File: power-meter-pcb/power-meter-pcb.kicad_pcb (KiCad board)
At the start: 4 copper layers, 23 x 51.5 mm, 56 parts, among them J1 Crank interconnect, J2 Debug, J3 USB4120-03-C_REVA, J4 Battery, J5 Side A, J6 Side B, Q3 AS2302, SW1 EN, SW2 BOOT, U1 TPS613221ADBV, U2 P3T1755, U4 TPD3E001DRLR, U7 ADS1232IPW, U8 ESP32-S3-MINI-1

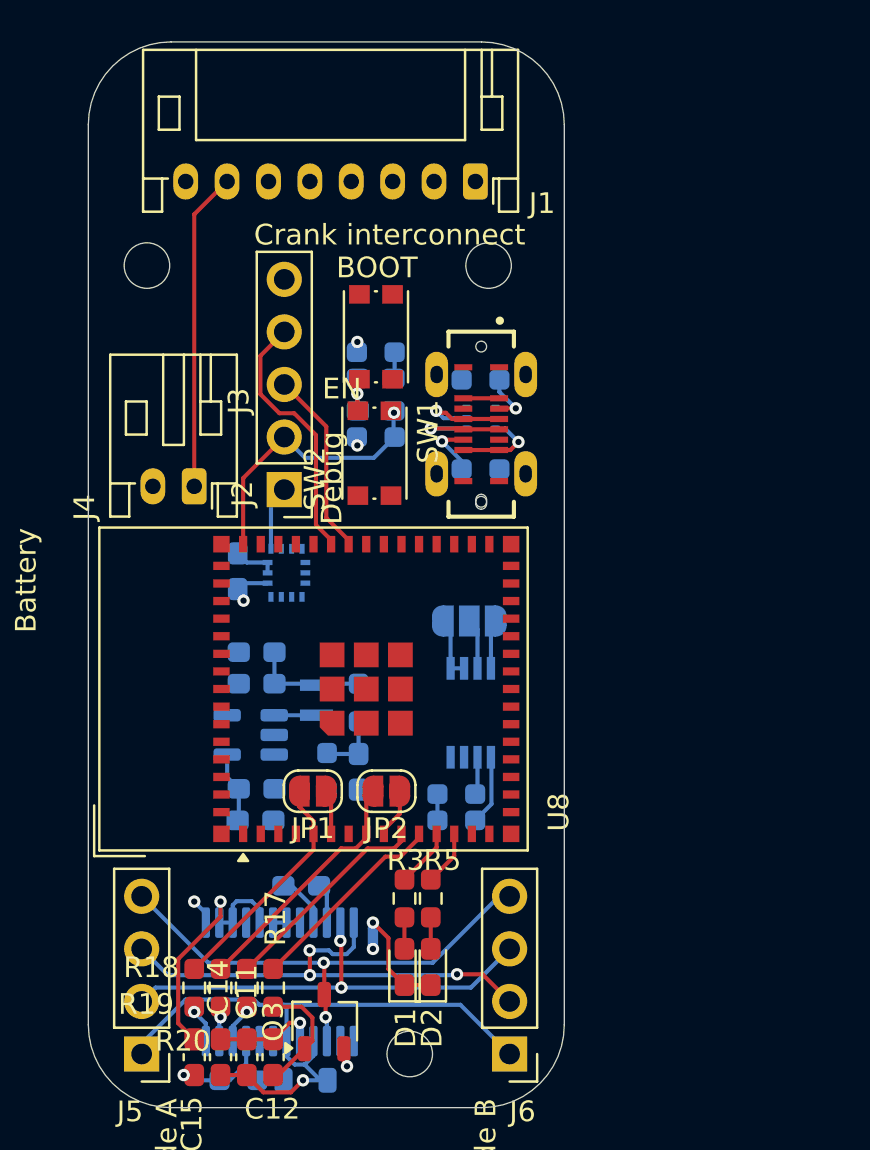
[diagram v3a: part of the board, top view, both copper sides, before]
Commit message: Board mostly routed, schematic page layout cleaned up
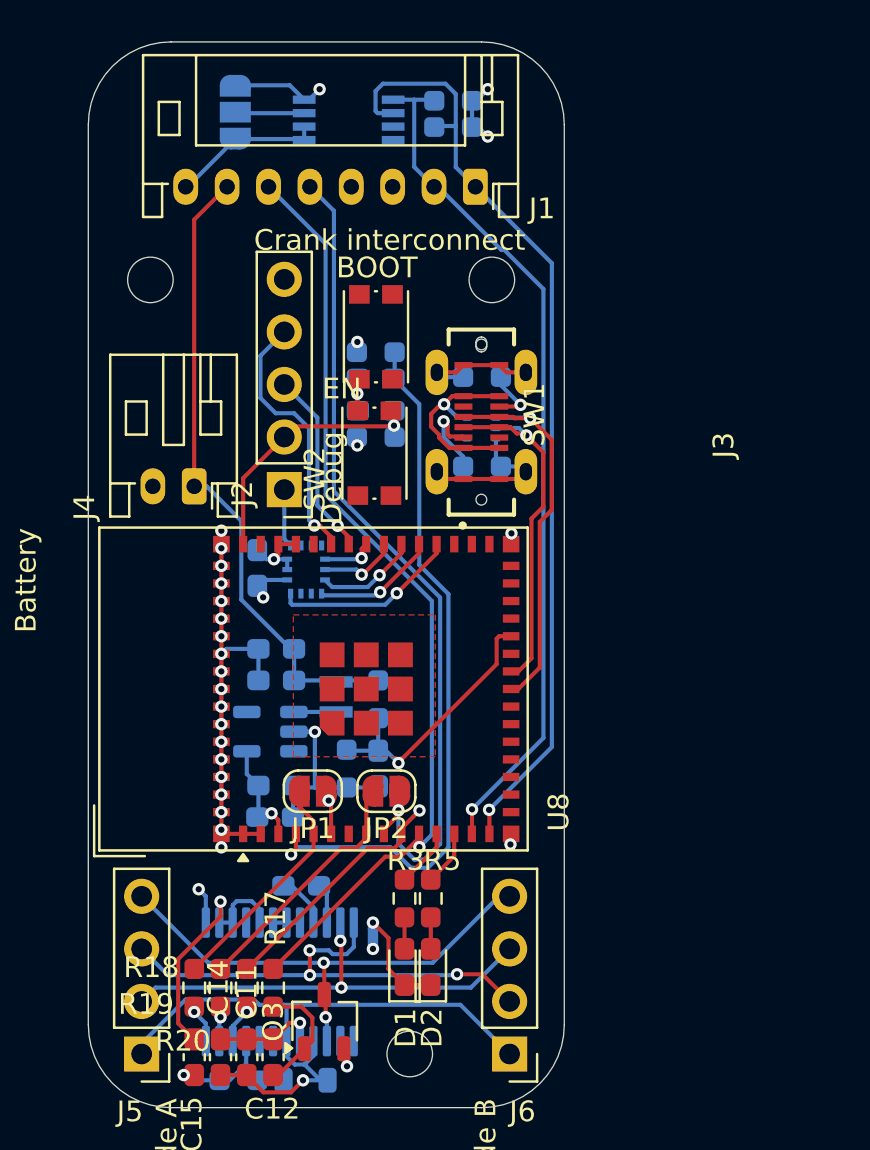
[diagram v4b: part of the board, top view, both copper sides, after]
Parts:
- moved R6 33.5 mm to (74.6, 51.2), turned to 180 degrees
- moved R4 33.5 mm to (74.6, 50.0), turned to 180 degrees
- moved U2 29.3 mm to (69.6, 50.9), turned to 180 degrees
- moved JP3 27.1 mm to (64.1, 50.5), turned to -90 degrees
- moved R11 4.45 mm to (76.0, 63.3), turned to 180 degrees
- moved R8 4.19 mm to (76.0, 67.6), turned to 0 degrees
- moved C10 0.96 mm to (66.1, 83.1)
- moved C16 0.96 mm to (65.2, 72.5)
- moved C5 0.96 mm to (66.1, 76.5)
- moved C7 0.96 mm to (66.1, 78.0)
- moved C8 0.96 mm to (66.0, 84.6)
- moved C9 0.96 mm to (71.0, 82.2)
- moved MT1 0.96 mm to (67.5, 72.6)
- moved R14 0.96 mm to (71.0, 78.9)
- moved R15 0.96 mm to (69.5, 82.2)
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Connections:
- R4 pad 2: /I2C.SDA -> /I2C.SCL
- R6 pad 2: /I2C.SCL -> /I2C.SDA
- U8 pad 14: unconnected-(U8-IO10-Pad14) -> /I2C.SCL
- U8 pad 15: unconnected-(U8-IO11-Pad15) -> /I2C.SDA
- U8 pad 34: unconnected-(U8-IO38-Pad34) -> /Accelerometer/Interrupt
- U8 pad 35: unconnected-(U8-IO39-Pad35) -> /Accelerometer/SPI.SDO
- U8 pad 36: unconnected-(U8-IO40-Pad36) -> /Accelerometer/SPI.SDI
- U8 pad 37: unconnected-(U8-IO41-Pad37) -> /Accelerometer/SPI.SCLK
- U8 pad 38: unconnected-(U8-IO42-Pad38) -> /Accelerometer/SPI.AC_CS
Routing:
- net GNDD: track 28.3 -> 76.8 mm, vias 3 -> 26
- net /I2C.SDA: track 1.82 -> 46.1 mm, vias 0 -> 1
- net /AMP2.DOUT: track 2.16 -> 43.2 mm, vias 0 -> 1
- net /AMP_PWDN: track 10.4 -> 49.9 mm, vias 0 -> 1
- net /AMP2.SCLK: track 2.38 -> 41.0 mm, vias 0 -> 1
- net /I2C.SCL: track 3.38 -> 41.7 mm, vias 0 -> 1
- net /Power save: track 9.87 -> 46.0 mm, vias 0 -> 1
- net /BOOT: track 1.29 -> 34.7 mm, vias 0 -> 1
- net +3.3V: track 20.1 -> 35.7 mm, vias 5 -> 9
- net /USB and power supply/USB.D_N: track 5.05 -> 19.5 mm
- net /USB and power supply/USB.D_P: track 4.82 -> 17.4 mm
- net +BATT: track 21.0 -> 31.3 mm
- net /USB and power supply/Battery voltage: track 3.11 -> 13.1 mm, vias 0 -> 1
- net /Accelerometer/Interrupt: track 0.00 -> 9.02 mm, vias 0 -> 1
- net /Accelerometer/SPI.SDO: track 0.00 -> 6.03 mm, vias 0 -> 1
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- added copper zone on F.Cu, net GNDD

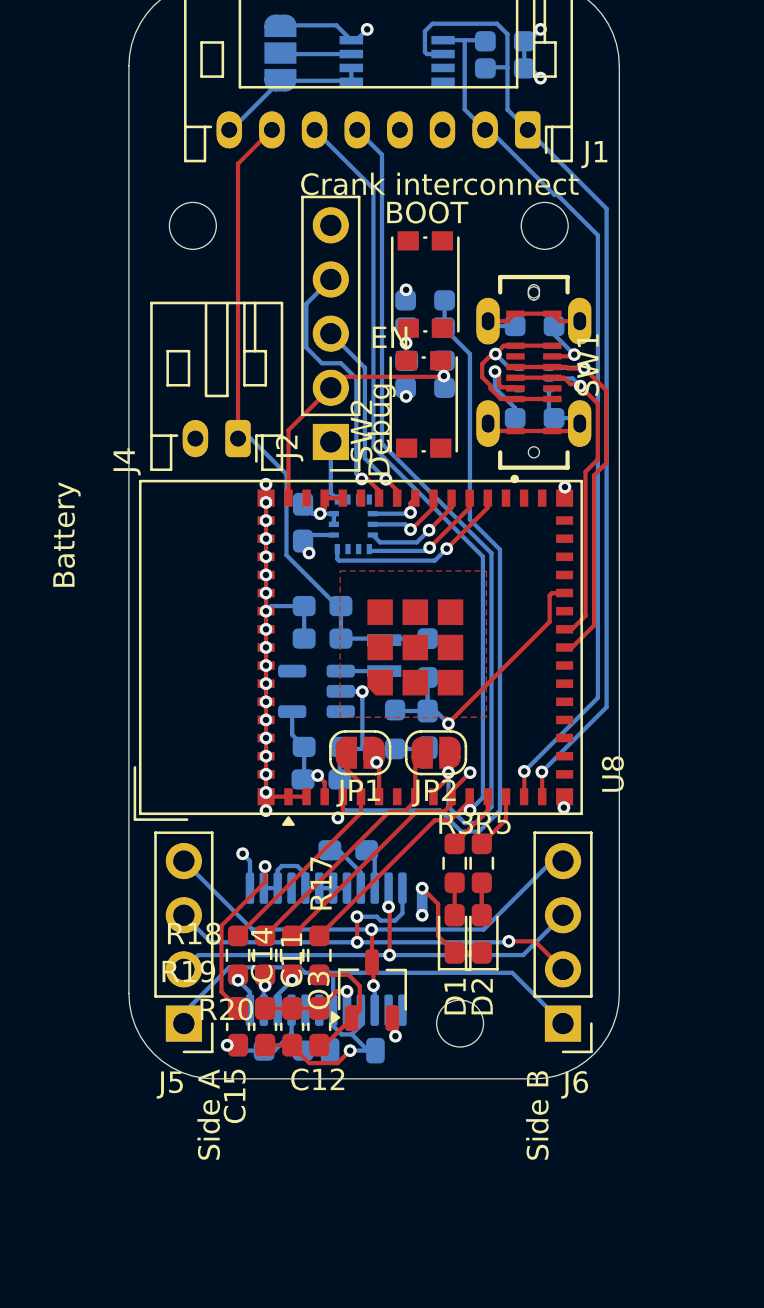
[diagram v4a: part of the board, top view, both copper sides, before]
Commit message: Silkscreen done
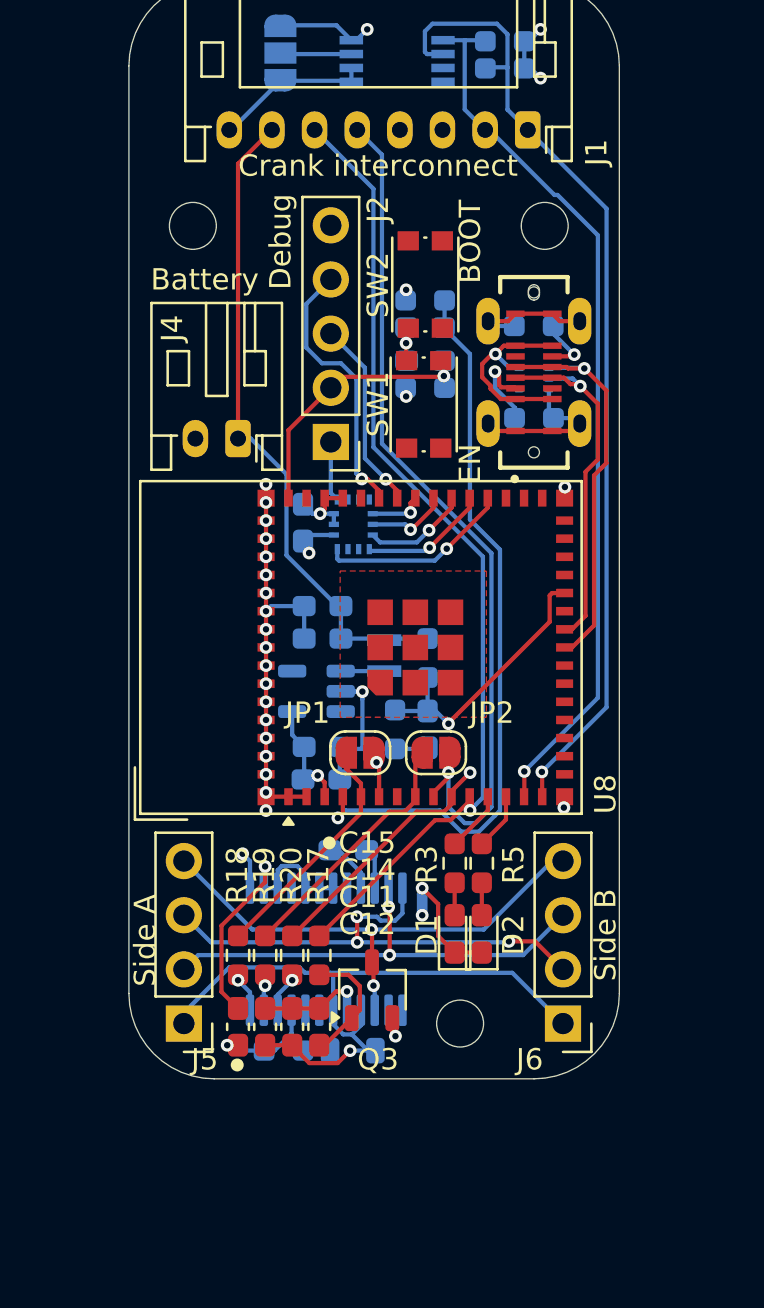
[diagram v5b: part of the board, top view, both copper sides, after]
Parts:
- moved G*** 50.6 mm to (75.2, 75.4), turned to -90 degrees
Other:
- board text added: "+B"
- board text added: "+V"
- board text added: "DOUT"
- board text added: "GND"
- board text added: "J. Gates & O. Varney, 2024"
- board text added: "PS"
- board text added: "PWDN"
- board text added: "SCL"
- board text added: "SCLK"
- board text added: "SDA"
- board text removed: "3.3V"
- board text removed: "G"
- board text removed: "Jotham Gates & Oscar Varney, 2024"

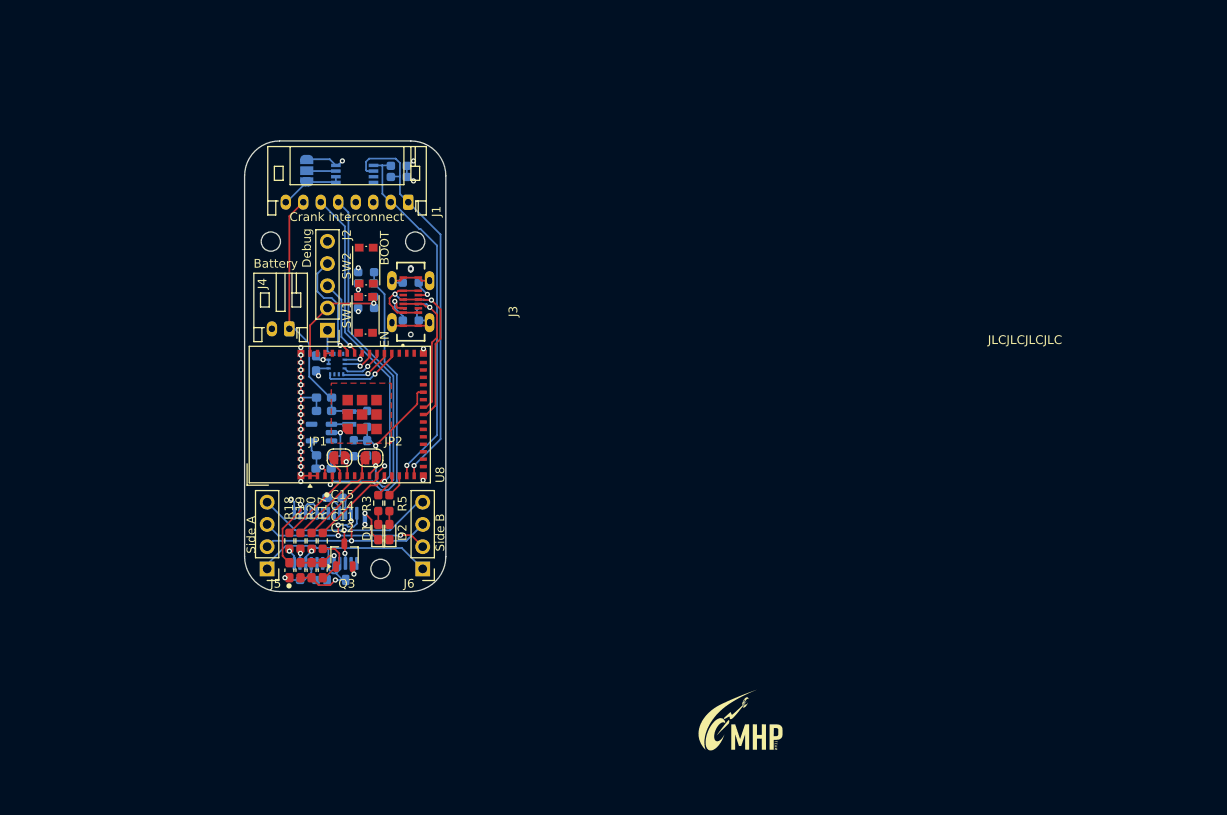
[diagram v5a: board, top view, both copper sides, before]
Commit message: Added date updating script.
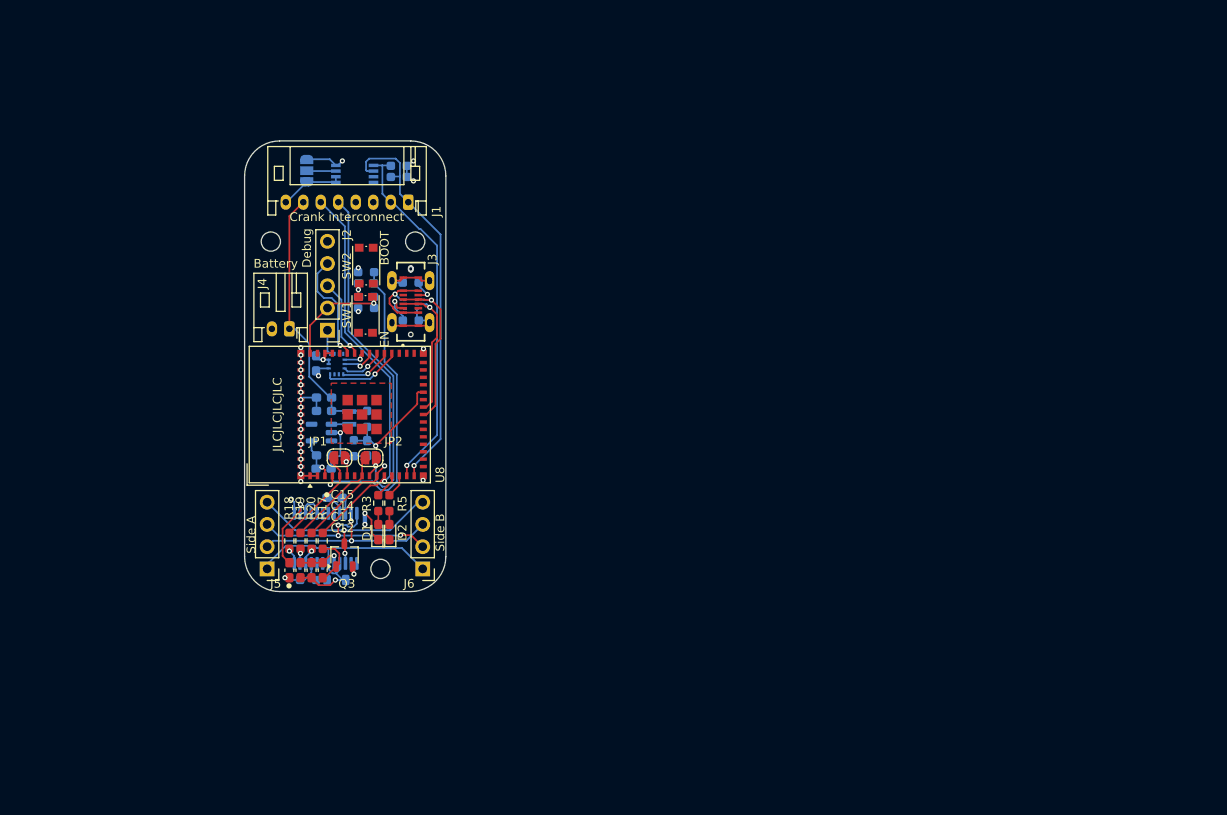
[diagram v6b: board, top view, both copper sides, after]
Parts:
- removed the G*** at (113.7, 113.3)

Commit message: Re-centred schematics, added header for spare GPIO pins, touched up logos
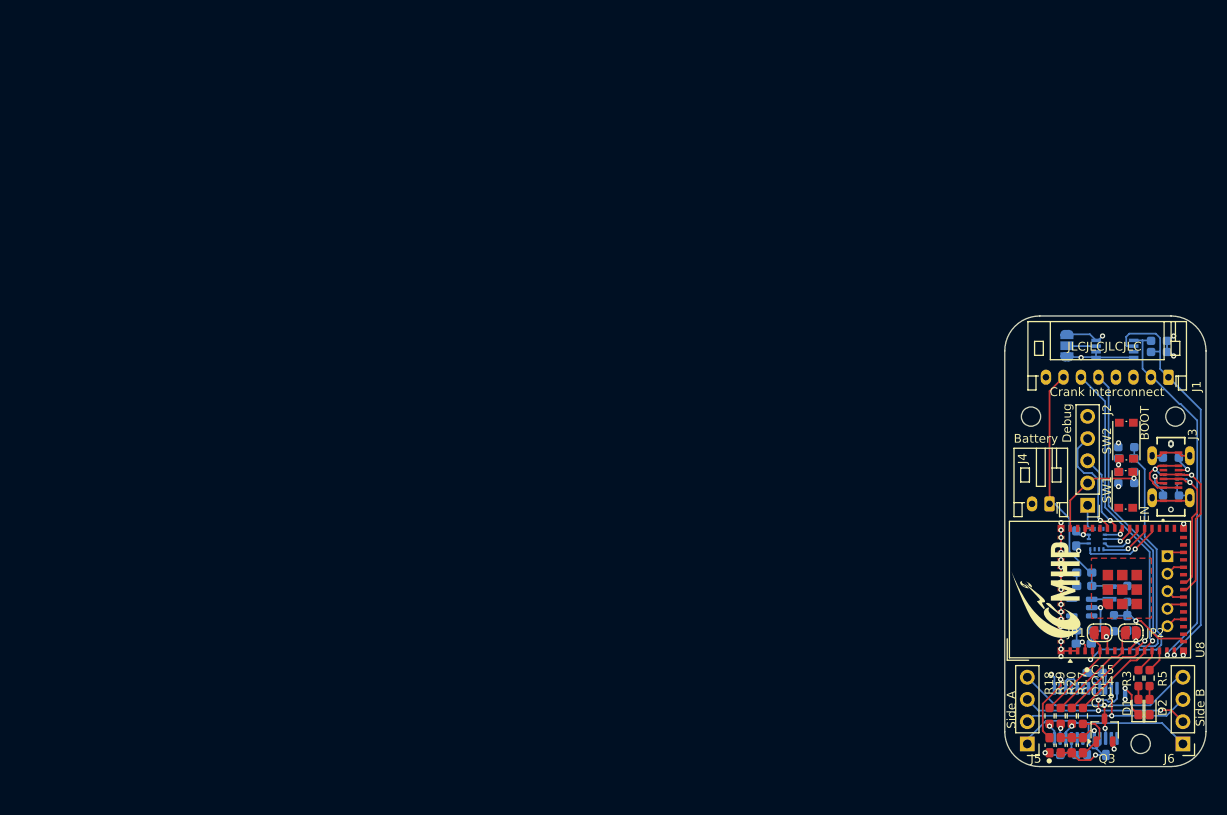
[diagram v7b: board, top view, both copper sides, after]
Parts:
- removed G***: LOGO, LOGO
- added J7: Spare GPIO pins, Connector_PinHeader_2.00mm:PinHeader_1x05_P2.00mm_Vertical, B.Cu at (162.5, 94.6)
- moved C10 89.2 mm to (153.0, 103.1)
- moved C12 89.2 mm to (152.8, 116.2)
- moved C13 89.2 mm to (154.2, 107.9)
- moved C14 89.2 mm to (150.3, 116.2)
- moved C5 89.2 mm to (153.0, 96.5)
- moved C7 89.2 mm to (153.0, 98.0)
- moved C8 89.2 mm to (152.9, 104.6)
- moved C9 89.2 mm to (157.9, 102.2)
- moved D2 89.2 mm to (160.4, 111.8)
- moved FB1 89.2 mm to (154.4, 117.3)
- moved H1 89.2 mm to (163.4, 78.6)
- moved J5 89.2 mm to (146.5, 116.0)
- moved J6 89.2 mm to (164.3, 116.0)
- moved L1 89.2 mm to (155.9, 98.8)
- moved R1 89.2 mm to (157.8, 86.2)
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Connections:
- C9 pad 1: /USB and power supply/Battery voltage -> /Battery voltage
- R14 pad 2: /USB and power supply/Battery voltage -> /Battery voltage
- R15 pad 1: /USB and power supply/Battery voltage -> /Battery voltage
- U8 pad 16: unconnected-(U8-IO12-Pad16) -> /Battery voltage
- U8 pad 19: unconnected-(U8-IO15-Pad19) -> /GPIO.15
- U8 pad 21: unconnected-(U8-IO17-Pad21) -> /GPIO.17
- U8 pad 22: unconnected-(U8-IO18-Pad22) -> /GPIO.18
- U8 pad 26: /USB and power supply/Battery voltage -> /GPIO.26
- U8 pad 28: unconnected-(U8-IO33-Pad28) -> /GPIO.33
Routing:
- net /USB and power supply/Battery voltage: track 13.1 -> 0.00 mm, vias 1 -> 0
- net /Battery voltage: track 0.00 -> 10.8 mm, vias 0 -> 1
- net /AMP2.DOUT: track 43.2 -> 48.5 mm
- net /AMP_PWDN: track 49.9 -> 53.4 mm
- net /AMP2.SCLK: track 41.0 -> 38.5 mm
- net /GPIO.15: track 0.00 -> 2.17 mm
- net /GPIO.26: track 0.00 -> 2.15 mm
- net /GPIO.18: track 0.00 -> 2.11 mm
- net /GPIO.17: track 0.00 -> 2.04 mm
- net /GPIO.33: track 0.00 -> 2.02 mm
- net GNDD: track 76.8 -> 77.9 mm, vias 26 -> 27
- net /Power save: track 46.0 -> 44.9 mm
- net /I2C.SCL: track 41.7 -> 42.7 mm
- net /I2C.SDA: track 46.1 -> 47.0 mm
- net /BOOT: track 34.7 -> 33.8 mm
